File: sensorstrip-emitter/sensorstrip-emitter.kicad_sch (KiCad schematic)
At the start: 6 parts, among them J1 Conn_01x02_MountingPin, J2 Conn_01x02_MountingPin

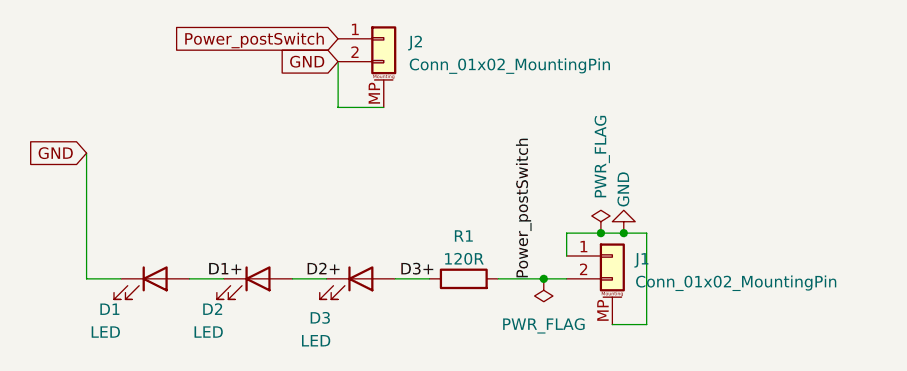
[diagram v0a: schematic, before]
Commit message: Rename sender / receiver boards to power-emitter and emitter
...hopefully this is clearer

Also some tidying of older boards
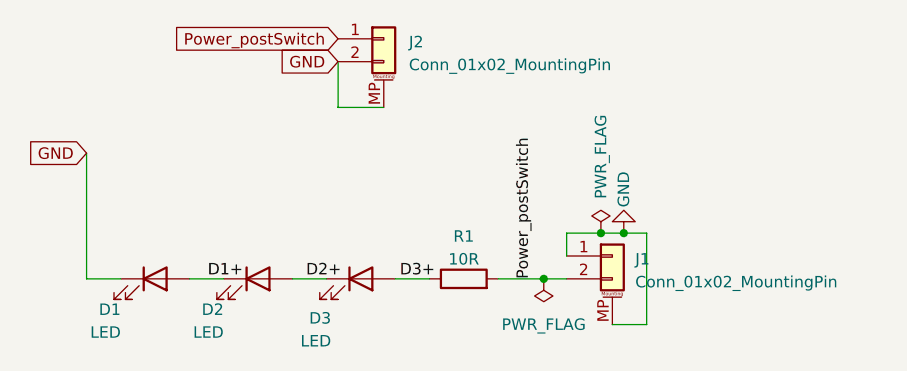
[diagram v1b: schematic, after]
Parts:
- R1: value 120R -> 10R
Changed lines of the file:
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@@
 			)
 		)
-		(property "Value" "120R"
+		(property "Value" "10R"
 			(at 101.6 89.2611 90)
 			(effects
